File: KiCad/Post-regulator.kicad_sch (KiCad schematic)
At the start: 104 parts, among them IC16 LTC2050HVCS8#PBF, IC17 TL072D, IC18 TL072D, IC19 SN74LVC1G3157DCKR, Q10 MMBT5401, Q11 MMBT5401, Q12 BCP56-16.115, Q13 MMBT5551, Q14 IRFP250NPBF, Q15 BCP56-16.115, Q16 BC857C, Q17 IRFI9Z34GPBF, Q18 PSMN0R9-25YLC, Q19 PSMN0R9-25YLC, Q9 MMBT5551

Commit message: r4B3 version: OE fixed, new LEDs for remote programming
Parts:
- added KK4: SP400-0.007-00-104, symbol PCM_EEZ_unsorted:TO247_Thermal_pad
- C100, C101: value N.C. -> 2n2
- C102, C99: value N.C. -> 47p
- C95: value 150p -> 330p; DigiKey 1276-1828-1-ND -> 1276-1189-1-ND; Mouser 710-885012007058 -> 80-C0805C331J5G; TME CC0805JRNPO9BN151 -> CL21C331JBANNNC
- C96: Mouser 710-885012007058 -> 80-C0805C151J5G
- KK3: DigiKey - -> 5496-SK9684SA-ND; LCSC (none) -> -
- R56: renamed from R55; Mouser 603-RC0603FR-10100RL -> 603-RT0603FRE07100RL
- R62: renamed from R61; Mouser 71-CRCW0805750RFKEB -> 71-CRCW0805750RFKEAC
- R70: renamed from R69; value 6K2 -> 6K8
- R72: renamed from R71; now fitted; now in the parts list
- R87: renamed from R86; value N.C. -> 10K
- R90: renamed from R89; value N.C. -> 10K
- R95: renamed from R94; DigiKey 511-1686-1-ND -> 846-GMR100HJBFA10L0CT-ND; LCSC (none) -> -; Mouser GMR100HTBFA10L0 -> GMR100HJBFA10L0
- RV2: Label (none) -> Uset
- RV3: Label (none) -> Iset
- ZD4: value PDZ6.2B -> BZT52C6V2; footprint PCM_EEZ_SMD:SOD-323_1P8X1P35_ONS-M -> PCM_EEZ_SMD:SOD123; DigiKey 1727-7771-1-ND -> 4878-BZT52C6V2CT-ND; LCSC C85400 -> C397931; Mouser 771-PDZ6.2BT/R -> 621-BZT52C6V2-13-F; TME PDZ6.2B-QX -> BZT52C6V2GW
- renumbered R99 to R100, R50 to R51, R51 to R52, R52 to R53, R53 to R54, R54 to R55, R56 to R57, R57 to R58, R58 to R59, R59 to R60, R60 to R61, R62 to R63, R63 to R64, R64 to R65, R65 to R66, R66 to R67, R67 to R68, R68 to R69, R70 to R71, R72 to R73, R73 to R74, R74 to R75, R75 to R76, R76 to R77, R77 to R78, R78 to R79, R79 to R80, R80 to R81, R81 to R82, R82 to R83, R83 to R84, R84 to R85, R85 to R86, R87 to R88, R88 to R89, R90 to R91, R91 to R92, R92 to R93, R93 to R94, R95 to R96, R96 to R97, R97 to R98, R98 to R99
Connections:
- net +3V3: now also R72.1
- net GND: no longer R72.1
- net -9V renamed -12V
- no-connect marks 4 -> 2
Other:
- note added: "Note 3.1: Q12, Q15 and R79 (if used) mounted on heatsink KK3 Note 3.2: Use power resistors with the lowest possible TCR (below ± 50 ppm/oC), e.g. GMR100HJBFA10L0"
- note removed: "0R"
- note removed: "0R022"
- note removed: "0R16"
- note removed: "18K"
- note removed: "1K8"
- note removed: "1K91"
- note removed: "220R"
- note removed: "2R2"
- note removed: "2n2"
- note removed: "825R"
- note removed: "82R"
- note removed: "Note 3.1: Q12, Q15 and R72 (if used) mounted on heatsink KK3 Note 3.2: Use power resistors with the lowest possible TCR (below ± 50 ppm/oC), e.g. GMR100HTBFA10L0"
- note removed: "SK510"

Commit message: BOM update
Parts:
- added KK10, KK7, KK8, KK9: M3X8/D7985B, symbol PCM_EEZ_unsorted:M3X8/D7985B
- added KK5, KK6: B3/BN2842, symbol PCM_EEZ_unsorted:B3/BN2842
- C100, C101: DigiKey (none) -> 399-C0805C222K5RAC7210TR-ND; Mouser (none) -> 80-C0805C222K5RACLR
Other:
- moved on the sheet: KK4

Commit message: EEPROM connected to H503 I2C bus
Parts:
- renumbered KK5 to KK10, KK9 to KK3, KK10 to KK4, KK7 to KK5, KK3 to KK7, KK4 to KK8, KK8 to KK9, R51 to R48, R52 to R49, R53 to R50, R54 to R51, R55 to R52, R56 to R53, R57 to R54, R58 to R55, R59 to R56, R60 to R57, R61 to R58, R62 to R59, R63 to R60, R64 to R61, R65 to R62, R66 to R63, R67 to R64, R68 to R65, R69 to R66, R70 to R67, R71 to R68, R72 to R69, R73 to R70, R74 to R71, R75 to R72, R76 to R73, R77 to R74, R78 to R75, R79 to R76, R80 to R77, R81 to R78, R82 to R79, R83 to R80, R84 to R81, R85 to R82, R86 to R83, R87 to R84, R88 to R85, R89 to R86, R90 to R87, R91 to R88, R92 to R89, R93 to R90, R94 to R91, R95 to R92, R96 to R93, R97 to R94, R98 to R95, R99 to R96, R100 to R97

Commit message: Vref tantalum capacitor removed
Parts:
- renumbered C99 to C100, C100 to C101, C101 to C102, C102 to C103, C78 to C79, C79 to C80, C80 to C81, C81 to C82, C82 to C83, C83 to C84, C84 to C85, C85 to C86, C86 to C87, C87 to C88, C88 to C89, C89 to C90, C90 to C91, C91 to C92, C92 to C93, C93 to C94, C94 to C95, C95 to C96, C96 to C97, C97 to C98, C98 to C99, R48 to R50, R49 to R51, R50 to R52, R51 to R53, R52 to R54, R53 to R55, R54 to R56, R55 to R57, R56 to R58, R57 to R59, R58 to R60, R59 to R61, R60 to R62, R61 to R63, R62 to R64, R63 to R65, R64 to R66, R65 to R67, R66 to R68, R67 to R69, R68 to R70, R69 to R71, R70 to R72, R71 to R73, R72 to R74, R73 to R75, R74 to R76, R75 to R77, R76 to R78, R77 to R79, R78 to R80, R79 to R81, R80 to R82, R81 to R83, R82 to R84, R83 to R85, R84 to R86, R85 to R87, R86 to R88, R87 to R89, R88 to R90, R89 to R91, R90 to R92, R91 to R93, R92 to R94, R93 to R95, R94 to R96, R95 to R97, R96 to R98, R97 to R99

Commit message: r4B4 (ADC replaced with ADS131A04)
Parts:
- renumbered C96 to C100, C97 to C101, C98 to C102, C99 to C103, C100 to C104, C101 to C105, C102 to C106, C103 to C107, C79 to C83, C80 to C84, C81 to C85, C82 to C86, C83 to C87, C84 to C88, C85 to C89, C86 to C90, C87 to C91, C88 to C92, C89 to C93, C90 to C94, C91 to C95, C92 to C96, C93 to C97, C94 to C98, C95 to C99

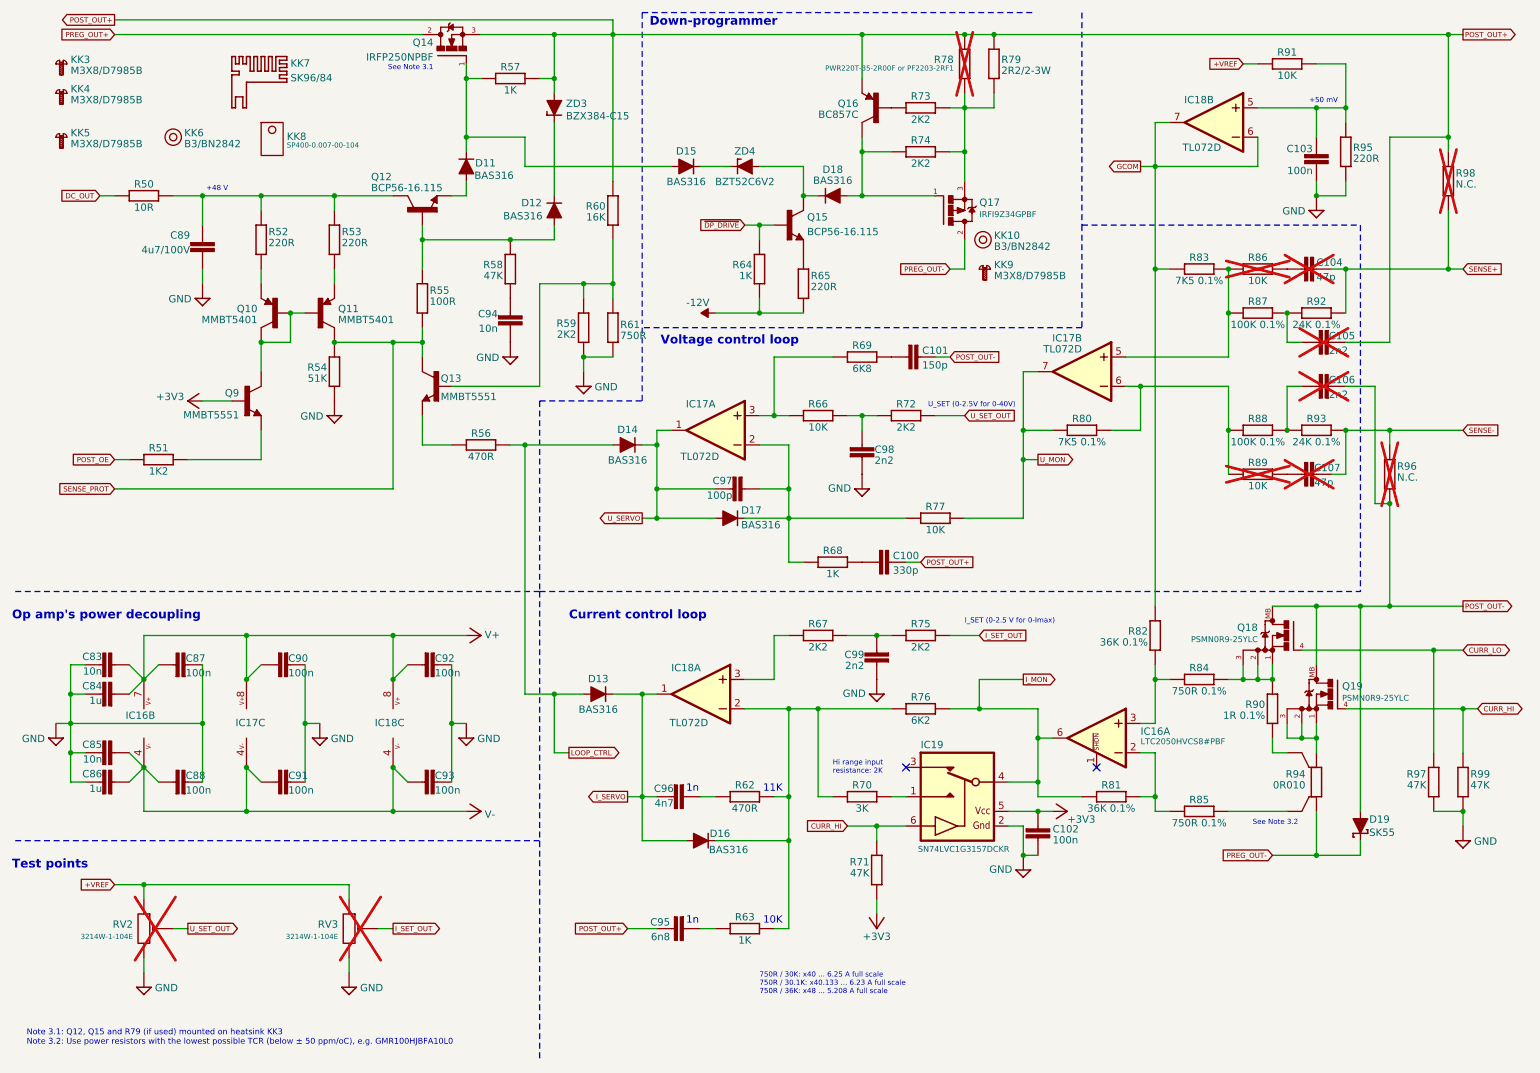
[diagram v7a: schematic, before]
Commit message: Additional 2 ch isolator added for OEP and temp sensor CS
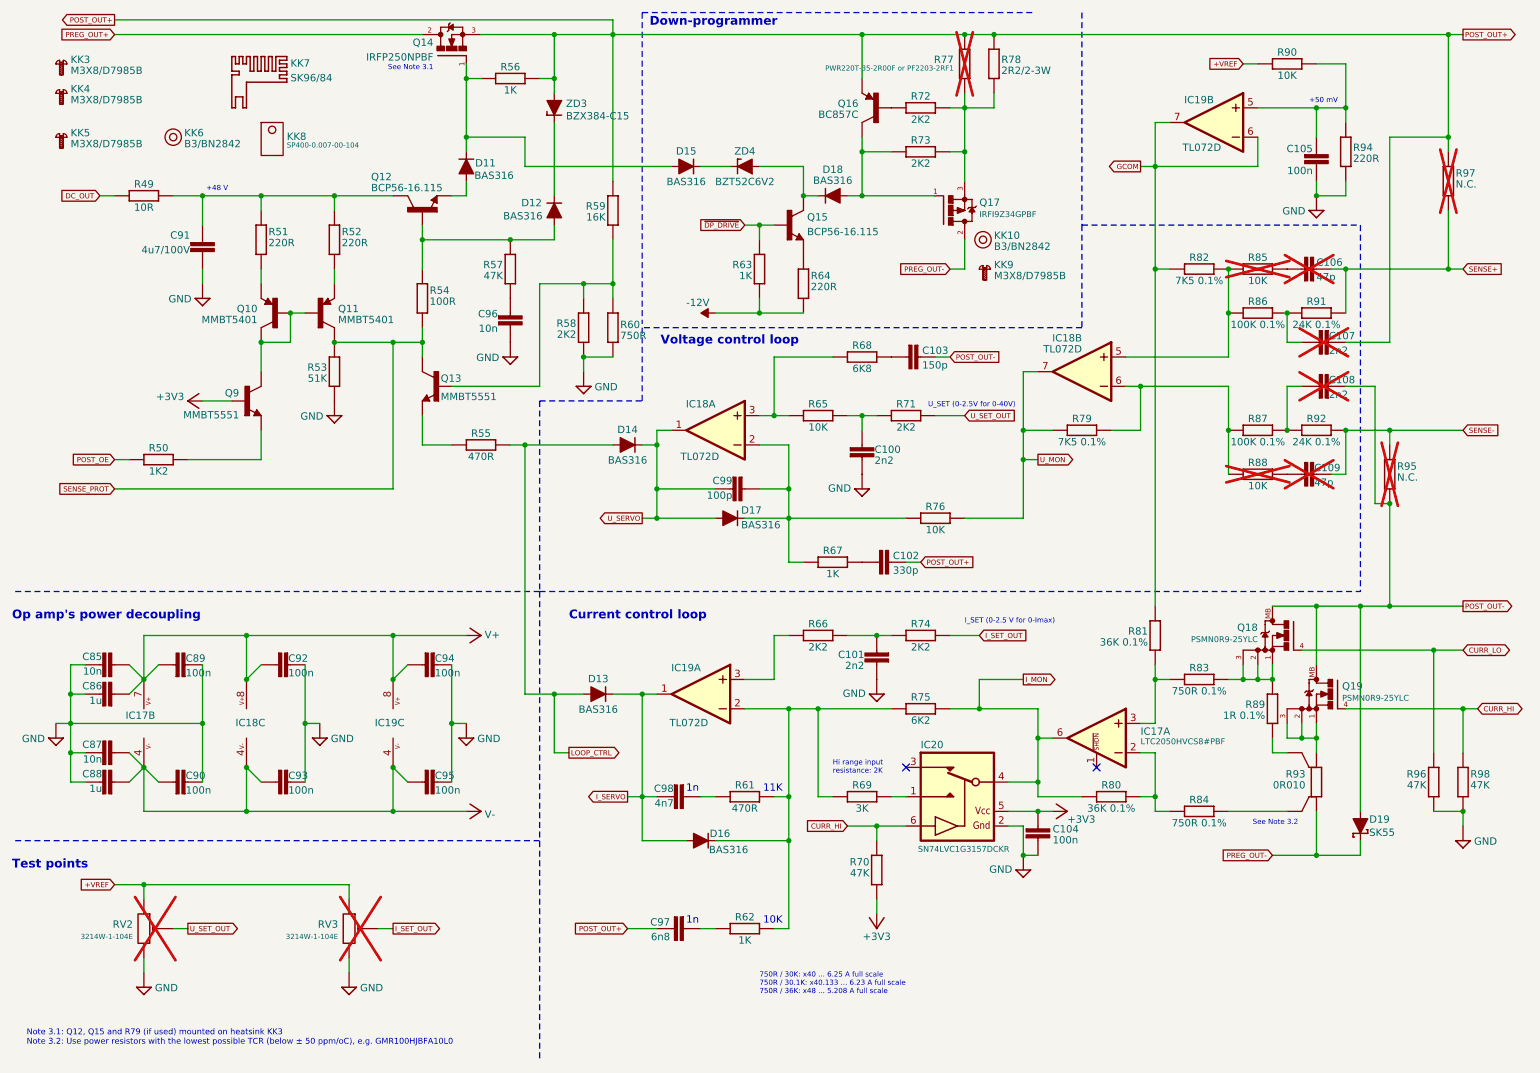
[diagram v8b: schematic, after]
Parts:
- renumbered C98 to C100, C99 to C101, C100 to C102, C101 to C103, C102 to C104, C103 to C105, C104 to C106, C105 to C107, C106 to C108, C107 to C109, C83 to C85, C84 to C86, C85 to C87, C86 to C88, C87 to C89, C88 to C90, C89 to C91, C90 to C92, C91 to C93, C92 to C94, C93 to C95, C94 to C96, C95 to C97, C96 to C98, C97 to C99, IC16 to IC17, IC17 to IC18, IC18 to IC19, IC19 to IC20, R50 to R49, R51 to R50, R52 to R51, R53 to R52, R54 to R53, R55 to R54, R56 to R55, R57 to R56, R58 to R57, R59 to R58, R60 to R59, R61 to R60, R62 to R61, R63 to R62, R64 to R63, R65 to R64, R66 to R65, R67 to R66, R68 to R67, R69 to R68, R70 to R69, R71 to R70, R72 to R71, R73 to R72, R74 to R73, R75 to R74, R76 to R75, R77 to R76, R78 to R77, R79 to R78, R80 to R79, R81 to R80, R82 to R81, R83 to R82, R84 to R83, R85 to R84, R86 to R85, R87 to R86, R88 to R87, R89 to R88, R90 to R89, R91 to R90, R92 to R91, R93 to R92, R94 to R93, R95 to R94, R96 to R95, R97 to R96, R98 to R97, R99 to R98
